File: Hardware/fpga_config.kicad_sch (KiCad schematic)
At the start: 0 parts

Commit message: Constraints for BGA layout
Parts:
- added U1: XC7A50T-CPG236, Package_BGA:Xilinx_CPG236, symbol FPGA_Xilinx_Artix7:XC7A50T-CPG236

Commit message: CSG325?
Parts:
- removed U1: XC7A50T-CPG236, Package_BGA:Xilinx_CPG236, symbol FPGA_Xilinx_Artix7:XC7A50T-CPG236
- added U2: XC7A35T-CSG325, Package_BGA:Xilinx_CSG325, symbol FPGA_Xilinx_Artix7:XC7A35T-CSG325

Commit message: PCIe
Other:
- moved on the sheet: U2E
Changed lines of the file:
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@@
 	(symbol
 		(lib_id "FPGA_Xilinx_Artix7:XC7A35T-CSG325")
-		(at 167.64 223.52 0)
+		(at 124.46 90.17 0)
 		(unit 5)
 		(body_style 1)
@@
 		(fields_autoplaced yes)
 		(property "Reference" "U2"
-			(at 134.62 225.4249 0)
+			(at 91.44 92.0749 0)
 			(show_name no)
 			(do_not_autoplace no)
@@
 		)
 		(property "Value" "XC7A35T-CSG325"
-			(at 134.62 227.9649 0)
+			(at 91.44 94.6149 0)
 			(show_name no)
 			(do_not_autoplace no)
@@
 		)
 		(property "Footprint" "Package_BGA:Xilinx_CSG325"
-			(at 167.64 223.52 0)
+			(at 124.46 90.17 0)
 			(hide yes)
 			(show_name no)
@@
 		)
 		(property "Datasheet" ""
-			(at 167.64 223.52 0)
+			(at 124.46 90.17 0)
 			(show_name no)
 			(do_not_autoplace no)
@@
 		)
 		(property "Description" "Artix 7 T 35 XC7A35T-CSG325"
-			(at 167.64 223.52 0)
+			(at 124.46 90.17 0)
 			(hide yes)
 			(show_name no)

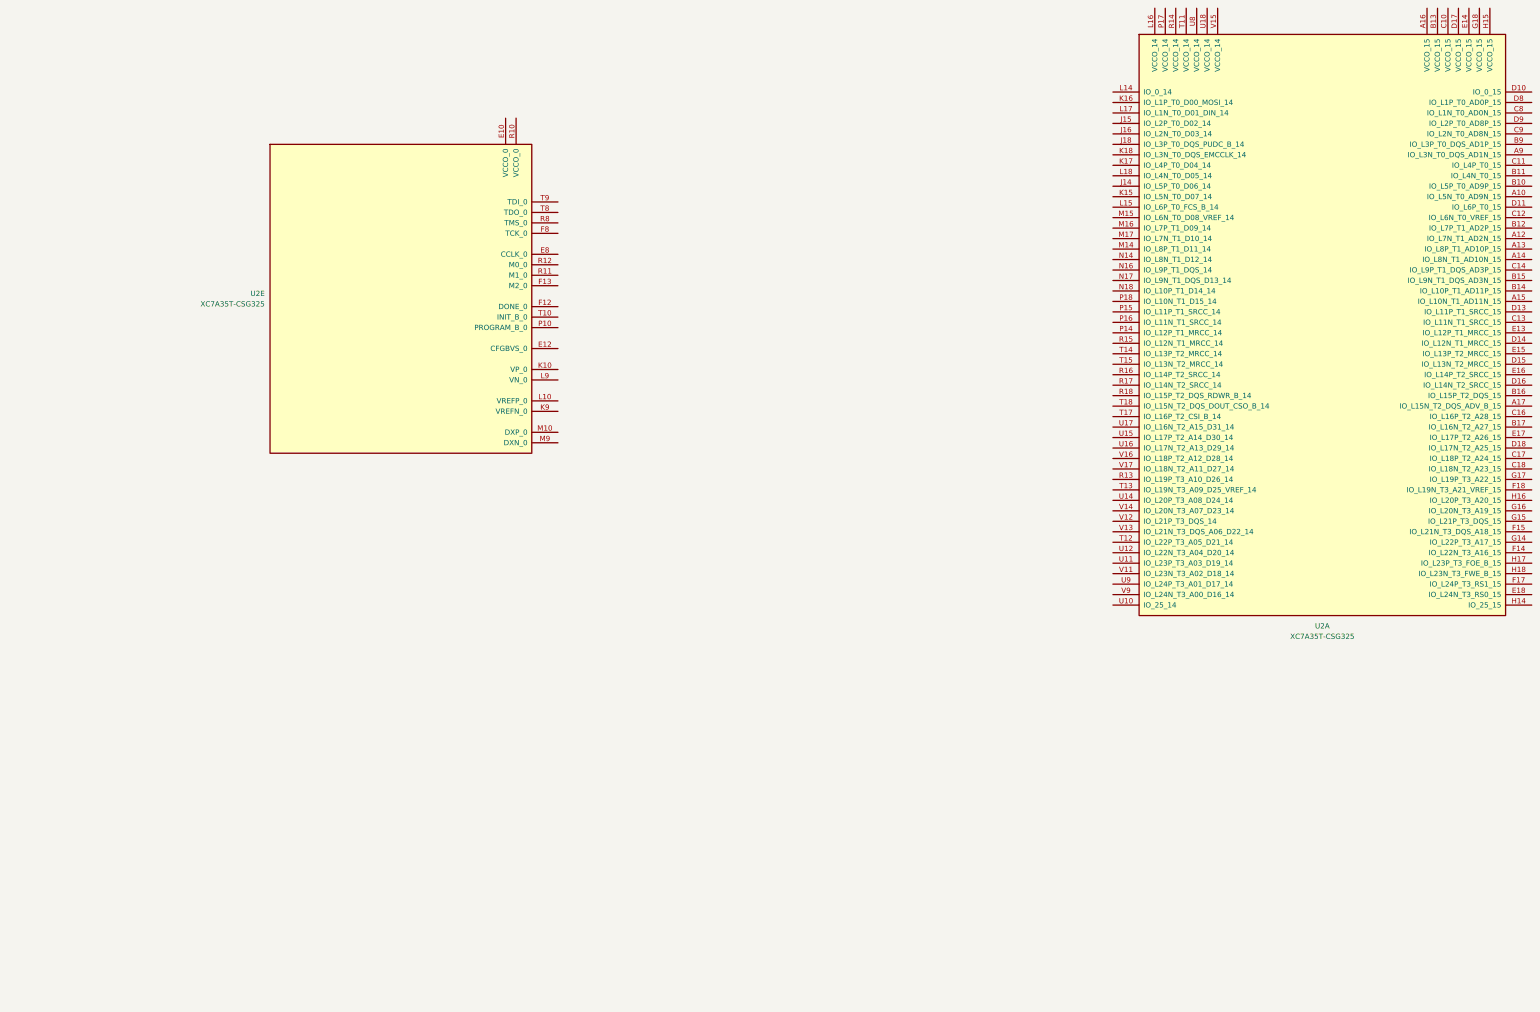
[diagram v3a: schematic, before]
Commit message: Added LGA connector, to be used for configuration interface
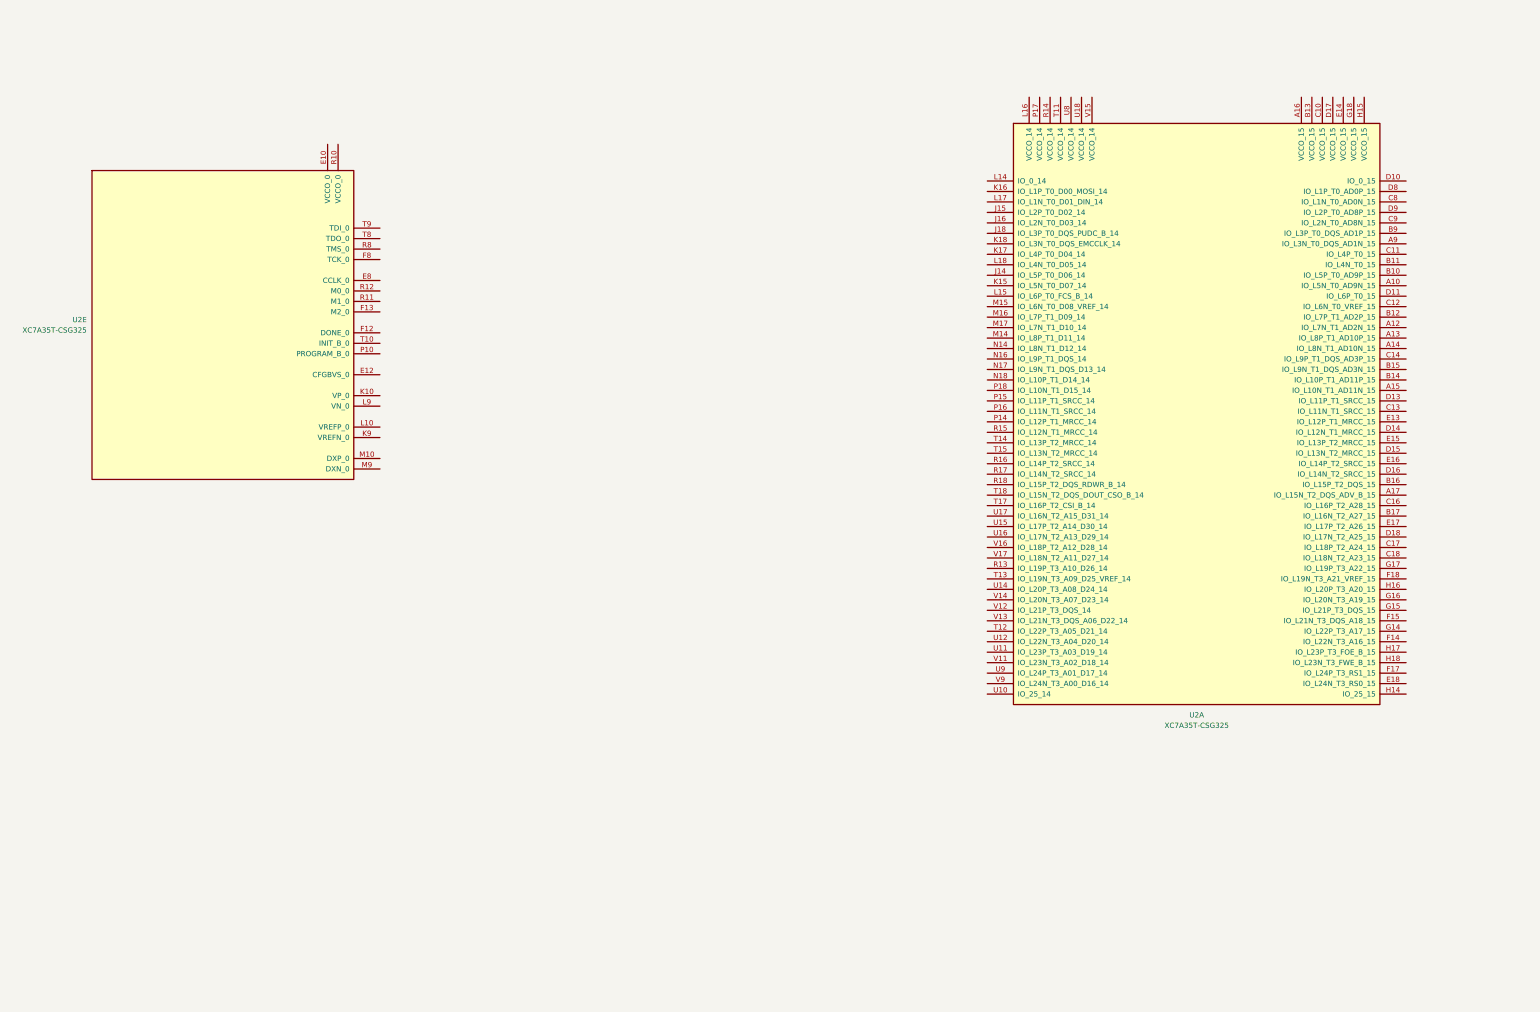
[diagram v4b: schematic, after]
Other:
- moved on the sheet: U2A, U2E
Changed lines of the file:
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@@
 	(symbol
 		(lib_id "FPGA_Xilinx_Artix7:XC7A35T-CSG325")
-		(at 347.98 96.52 0)
+		(at 317.5 118.11 0)
 		(unit 1)
 		(body_style 1)
@@
 		(fields_autoplaced yes)
 		(property "Reference" "U2"
-			(at 347.98 172.72 0)
+			(at 317.5 194.31 0)
 			(show_name no)
 			(do_not_autoplace no)
@@
 		)
 		(property "Value" "XC7A35T-CSG325"
-			(at 347.98 175.26 0)
+			(at 317.5 196.85 0)
 			(show_name no)
 			(do_not_autoplace no)
@@
 		)
 		(property "Footprint" "Package_BGA:Xilinx_CSG325"
-			(at 347.98 96.52 0)
+			(at 317.5 118.11 0)
 			(hide yes)
 			(show_name no)
@@
 		)
 		(property "Datasheet" ""
-			(at 347.98 96.52 0)
+			(at 317.5 118.11 0)
 			(show_name no)
 			(do_not_autoplace no)
@@
 		)
 		(property "Description" "Artix 7 T 35 XC7A35T-CSG325"
-			(at 347.98 96.52 0)
+			(at 317.5 118.11 0)
 			(hide yes)
 			(show_name no)
@@
 	(symbol
 		(lib_id "FPGA_Xilinx_Artix7:XC7A35T-CSG325")
-		(at 124.46 90.17 0)
+		(at 81.28 96.52 0)
 		(unit 5)
 		(body_style 1)
@@
 		(fields_autoplaced yes)
 		(property "Reference" "U2"
-			(at 91.44 92.0749 0)
+			(at 48.26 98.4249 0)
 			(show_name no)
 			(do_not_autoplace no)
@@
 		)
 		(property "Value" "XC7A35T-CSG325"
-			(at 91.44 94.6149 0)
+			(at 48.26 100.9649 0)
 			(show_name no)
 			(do_not_autoplace no)
@@
 		)
 		(property "Footprint" "Package_BGA:Xilinx_CSG325"
-			(at 124.46 90.17 0)
+			(at 81.28 96.52 0)
 			(hide yes)
 			(show_name no)
@@
 		)
 		(property "Datasheet" ""
-			(at 124.46 90.17 0)
+			(at 81.28 96.52 0)
 			(show_name no)
 			(do_not_autoplace no)
@@
 		)
 		(property "Description" "Artix 7 T 35 XC7A35T-CSG325"
-			(at 124.46 90.17 0)
+			(at 81.28 96.52 0)
 			(hide yes)
 			(show_name no)

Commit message: Found the global labels
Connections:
- net at U2.A16 (VCCO_15): now also U2.B13 (VCCO_15), U2.C10 (VCCO_15), U2.D17 (VCCO_15), U2.E14 (VCCO_15), U2.G18 (VCCO_15), U2.H15 (VCCO_15)
- net at U2.L16 (VCCO_14): now also U2.P17 (VCCO_14), U2.R14 (VCCO_14), U2.T11 (VCCO_14), U2.U18 (VCCO_14), U2.U8 (VCCO_14), U2.V15 (VCCO_14)
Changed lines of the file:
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@@
 	(generator_version "10.0")
 	(paper "B")
+	(junction
+		(at 347.98 44.45)
+		(diameter 0)
+		(color 0 0 0 0)
+	)
+	(junction
+		(at 289.56 44.45)
+		(diameter 0)
+		(color 0 0 0 0)
+	)
+	(junction
+		(at 284.48 44.45)
+		(diameter 0)
+		(color 0 0 0 0)
+	)
+	(junction
+		(at 287.02 44.45)
+		(diameter 0)
+		(color 0 0 0 0)
+	)
+	(junction
+		(at 353.06 44.45)
+		(diameter 0)
+		(color 0 0 0 0)
+	)
+	(junction
+		(at 350.52 44.45)
+		(diameter 0)
+		(color 0 0 0 0)
+	)
+	(junction
+		(at 345.44 44.45)
+		(diameter 0)
+		(color 0 0 0 0)
+	)
+	(junction
+		(at 279.4 44.45)
+		(diameter 0)
+		(color 0 0 0 0)
+	)
+	(junction
+		(at 281.94 44.45)
+		(diameter 0)
+		(color 0 0 0 0)
+	)
+	(junction
+		(at 355.6 44.45)
+		(diameter 0)
+		(color 0 0 0 0)
+	)
+	(wire
+		(pts
+			(xy 347.98 44.45) (xy 350.52 44.45)
+		)
+		(stroke
+			(width 0)
+			(type default)
+		)
+	)
+	(wire
+		(pts
+			(xy 350.52 44.45) (xy 353.06 44.45)
+		)
+		(stroke
+			(width 0)
+			(type default)
+		)
+	)
+	(wire
+		(pts
+			(xy 345.44 44.45) (xy 347.98 44.45)
+		)
+		(stroke
+			(width 0)
+			(type default)
+		)
+	)
+	(wire
+		(pts
+			(xy 289.56 44.45) (xy 292.1 44.45)
+		)
+		(stroke
+			(width 0)
+			(type default)
+		)
+	)
+	(wire
+		(pts
+			(xy 276.86 44.45) (xy 279.4 44.45)
+		)
+		(stroke
+			(width 0)
+			(type default)
+		)
+	)
+	(wire
+		(pts
+			(xy 279.4 44.45) (xy 281.94 44.45)
+		)
+		(stroke
+			(width 0)
+			(type default)
+		)
+	)
+	(wire
+		(pts
+			(xy 287.02 44.45) (xy 289.56 44.45)
+		)
+		(stroke
+			(width 0)
+			(type default)
+		)
+	)
+	(wire
+		(pts
+			(xy 342.9 44.45) (xy 345.44 44.45)
+		)
+		(stroke
+			(width 0)
+			(type default)
+		)
+	)
+	(wire
+		(pts
+			(xy 355.6 44.45) (xy 358.14 44.45)
+		)
+		(stroke
+			(width 0)
+			(type default)
+		)
+	)
+	(wire
+		(pts
+			(xy 353.06 44.45) (xy 355.6 44.45)
+		)
+		(stroke
+			(width 0)
+			(type default)
+		)
+	)
+	(wire
+		(pts
+			(xy 284.48 44.45) (xy 287.02 44.45)
+		)
+		(stroke
+			(width 0)
+			(type default)
+		)
+	)
+	(wire
+		(pts
+			(xy 281.94 44.45) (xy 284.48 44.45)
+		)
+		(stroke
+			(width 0)
+			(type default)
+		)
+	)
 	(symbol
 		(lib_id "FPGA_Xilinx_Artix7:XC7A35T-CSG325")
